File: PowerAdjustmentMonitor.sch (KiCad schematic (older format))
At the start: 11 parts

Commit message: Put the power schematic in the wrong sub-module (PowerAdjustmentMonitor)
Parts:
- removed C? (x2): C, ~, symbol C
- removed F? (x4): FUSE, ~, symbol FUSE
- removed L? (x2): INDUCTOR, ~, symbol INDUCTOR
- removed P?: CONN_12X2, symbol CONN_12X2
- removed R?: R, ~, symbol R
- removed SW?: SWITCH_INV, ~, symbol SWITCH_INV

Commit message: 3.7 Understanding The Power Control, Conditioning And Monitoring Module     Prior to addition of adjustable resistor. Acidently did save-whole-project
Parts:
- added JP? (x3): JUMPER, symbol JUMPER
- added R? (x10): R, symbol R
- added U? (x2): 7805, symbol 7805
- added U? (x2): LM317K, TO-3, symbol LM317K
- added U? (x2): LM324, symbol LM324
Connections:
- net labels added: +12V, +3.3V, +5V, -12V, 3V3_MON, 5V5_MON, AGND, FE_V+, FE_V-, GND, V+_ADJ_MON, V+_CURR_MON, V+_MON, V-_ADJ, V-_ADJ_MON, V-_CURR_MON, V-_MON
- wire segments 0 -> 87

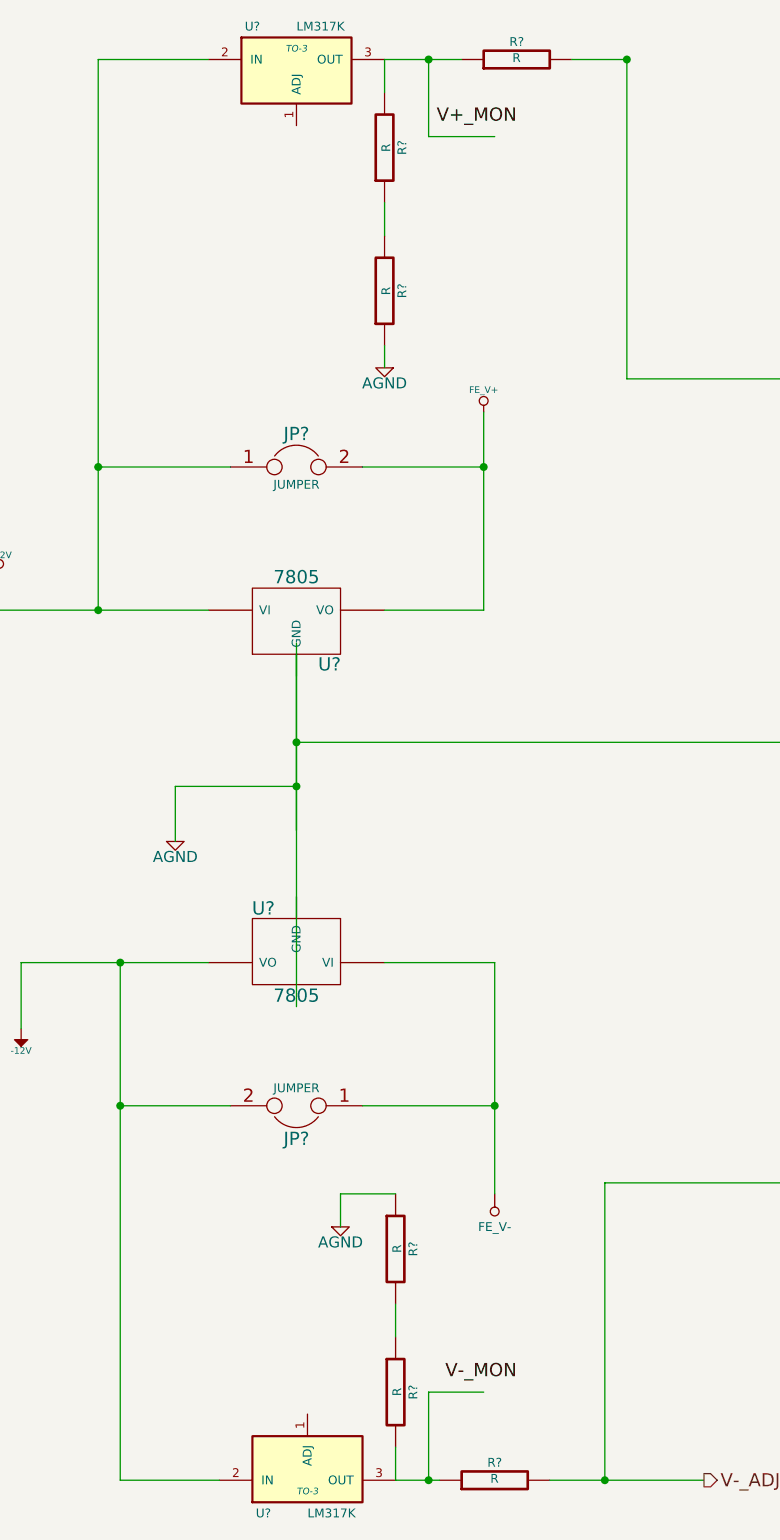
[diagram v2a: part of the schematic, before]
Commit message: Added variable resistor(s) to LM317's output
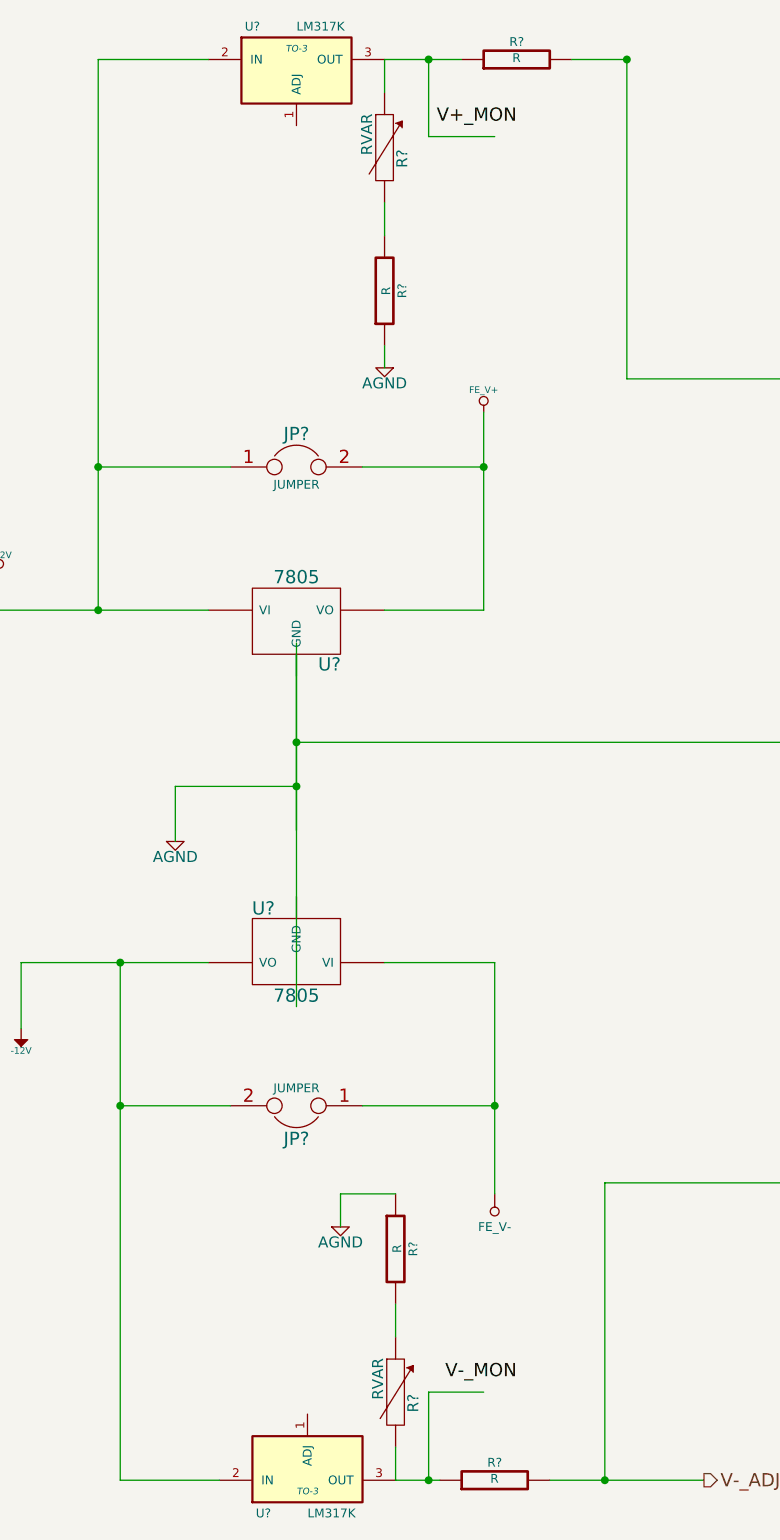
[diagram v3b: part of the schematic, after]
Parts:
- removed R? (x2): R, symbol R
- added R? (x2): RVAR, symbol RVAR
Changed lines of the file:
@@
-$Comp
-L R R?
-U 1 1 52F50F67
-P 4300 6850
-F 0 "R?" V 4380 6850 40  0000 C CNN
-F 1 "R" V 4307 6851 40  0000 C CNN
-F 2 "" V 4230 6850 30  0000 C CNN
-F 3 "" H 4300 6850 30  0000 C CNN
-	1    4300 6850
-	1    0    0    -1
-$EndComp
 $Comp
 L R R?
@@
 $Comp
 L R R?
-U 1 1 52F51722
-P 4250 1200
-F 0 "R?" V 4330 1200 40  0000 C CNN
-F 1 "R" V 4257 1201 40  0000 C CNN
-F 2 "" V 4180 1200 30  0000 C CNN
-F 3 "" H 4250 1200 30  0000 C CNN
-	1    4250 1200
-	1    0    0    1
-$EndComp
-$Comp
-L R R?
 U 1 1 52F51728
 P 4250 1850
@@
 Text Label 8950 6100 2    60   ~ 0
 V-_MON
+$Comp
+L RVAR R?
+U 1 1 52F526E6
+P 4300 6850
+F 0 "R?" V 4380 6800 50  0000 C CNN
+F 1 "RVAR" V 4220 6910 50  0000 C CNN
+F 2 "" H 4300 6850 60  0000 C CNN
+F 3 "" H 4300 6850 60  0000 C CNN
+	1    4300 6850
+	1    0    0    -1
+$EndComp
+$Comp
+L RVAR R?
+U 1 1 52F526F3
+P 4250 1200
+F 0 "R?" V 4330 1150 50  0000 C CNN
+F 1 "RVAR" V 4170 1260 50  0000 C CNN
+F 2 "" H 4250 1200 60  0000 C CNN
+F 3 "" H 4250 1200 60  0000 C CNN
+	1    4250 1200
+	1    0    0    -1
+$EndComp
 $EndSCHEMATC

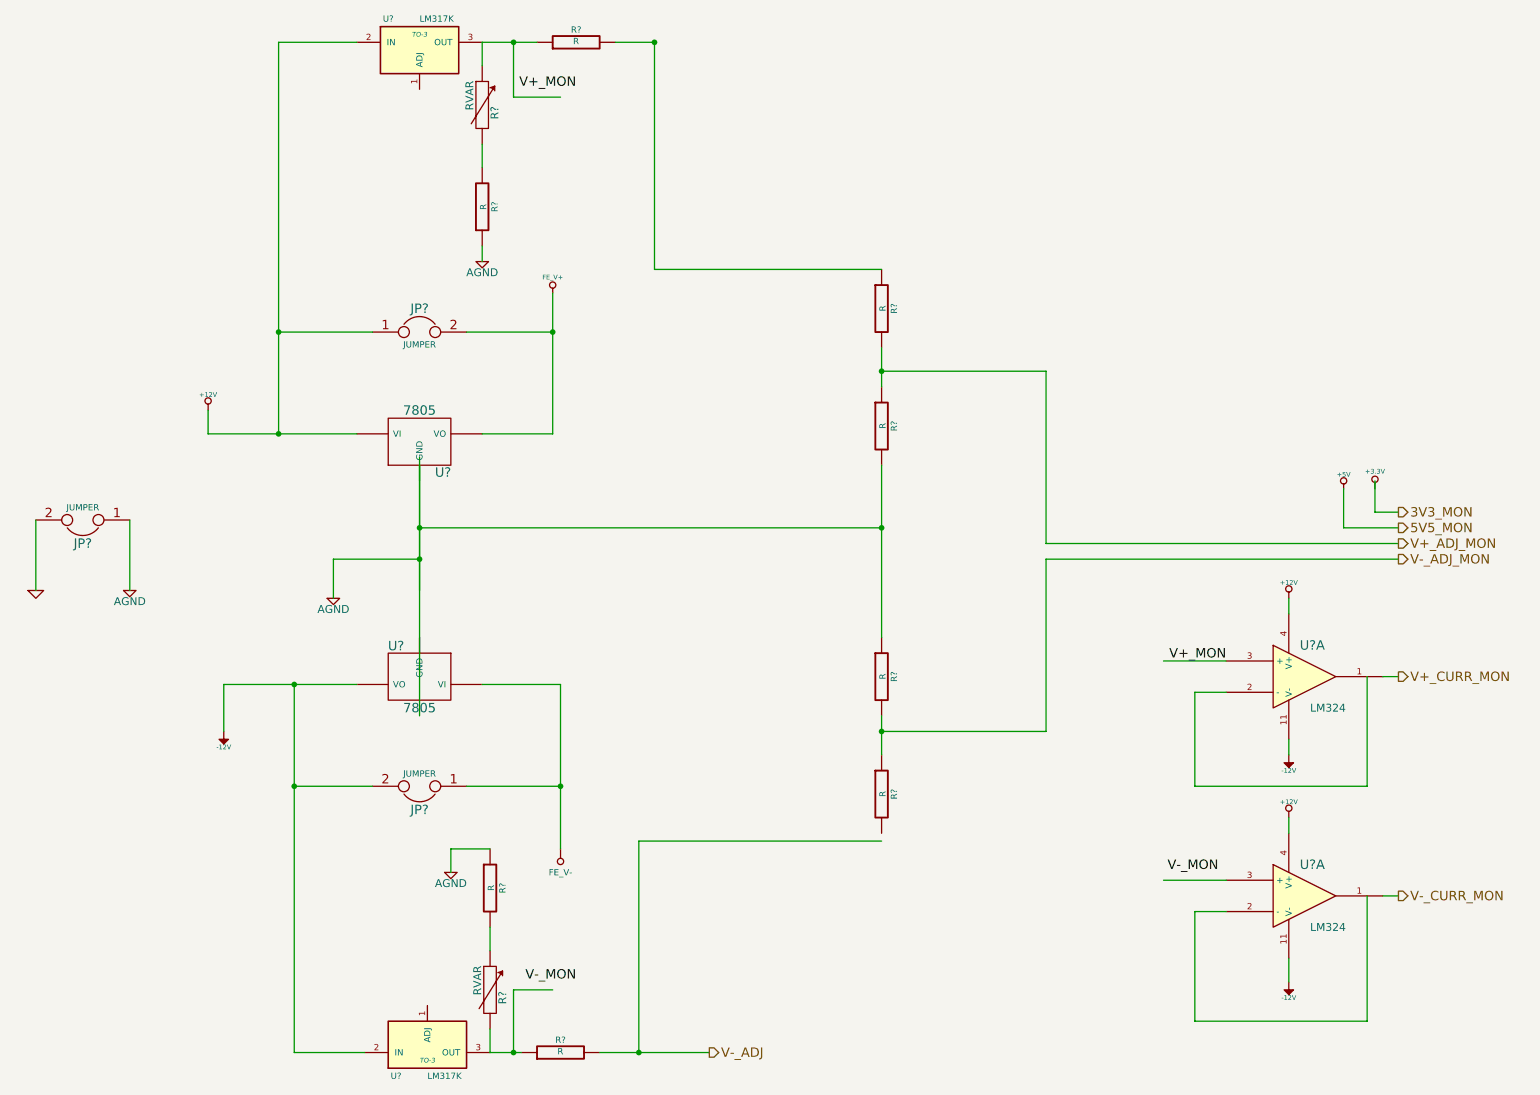
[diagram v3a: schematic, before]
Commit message: Forgot the V+_ADJ pin, fixed
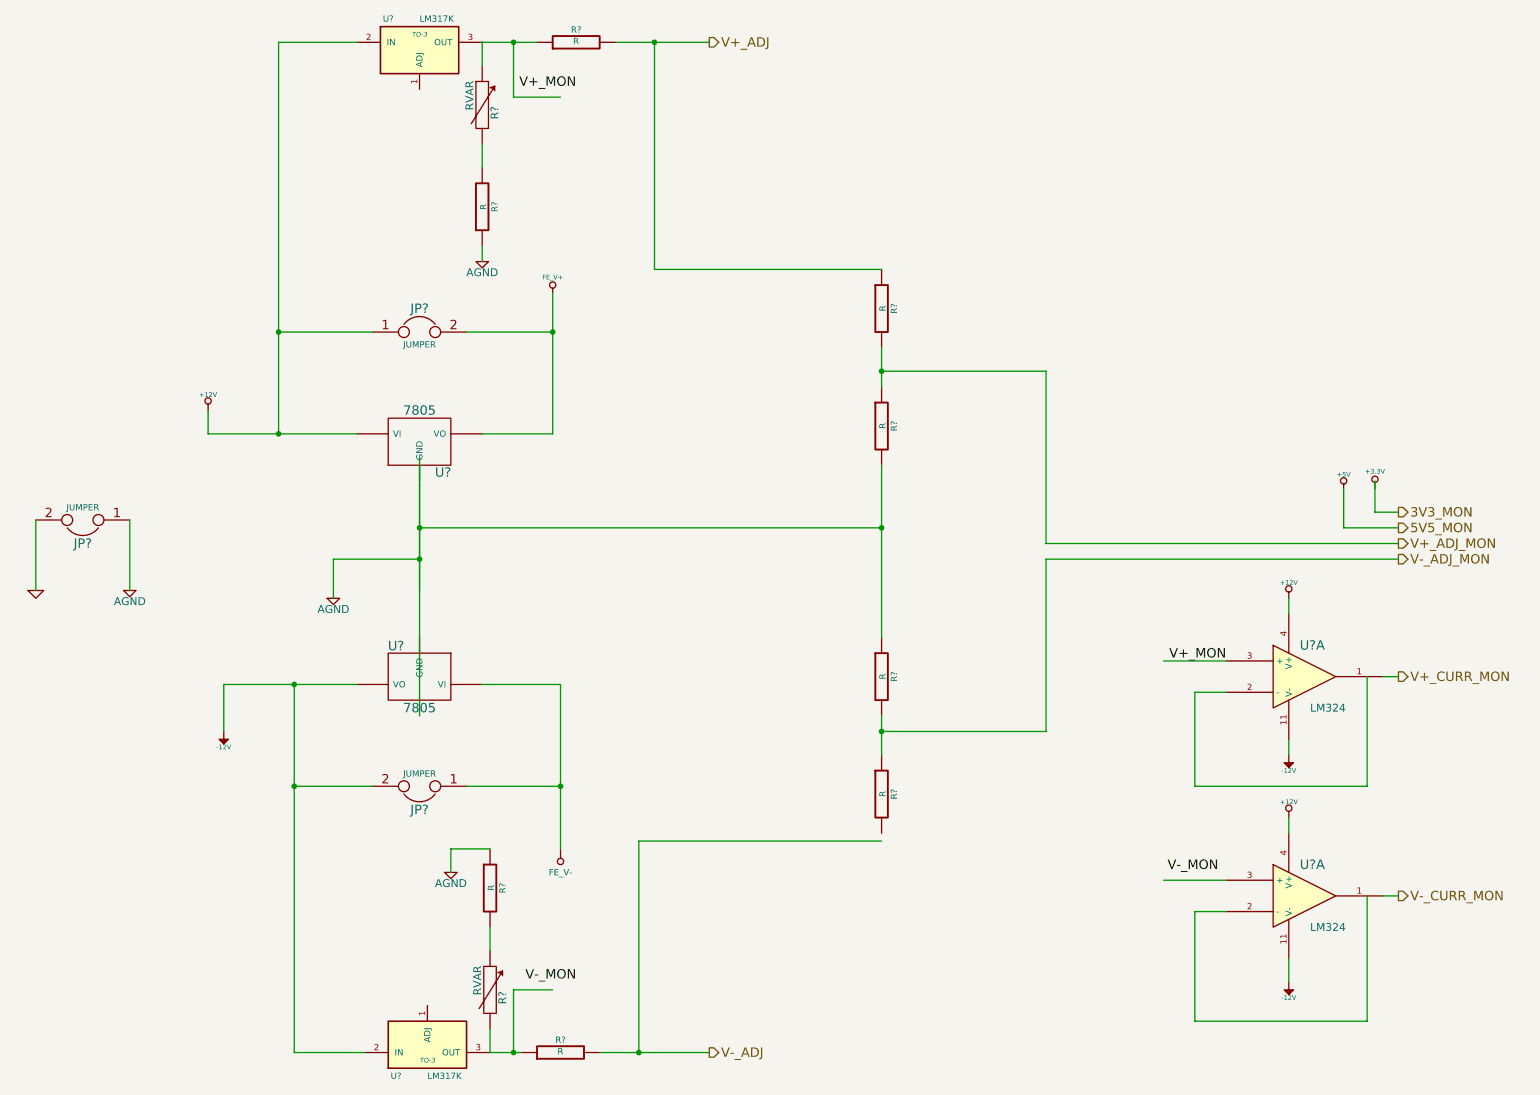
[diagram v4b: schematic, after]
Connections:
- net labels added: V+_ADJ
- wire segments 87 -> 71
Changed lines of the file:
@@
 	3550 2650 2950 2650
 Wire Wire Line
-	2950 800  2950 2650
-Wire Wire Line
-	2950 2650 2950 3300
-Wire Wire Line
-	2500 3300 2950 3300
-Wire Wire Line
-	2950 3300 3450 3300
+	2950 800  2950 3300
+Wire Wire Line
+	2500 3300 3450 3300
 Wire Wire Line
 	4150 2650 4700 2650
 Wire Wire Line
-	4700 2400 4700 2650
-Wire Wire Line
-	4700 2650 4700 3300
+	4700 2400 4700 3300
 Wire Wire Line
 	4700 3300 4250 3300
 Wire Wire Line
-	3850 3450 3850 3900
-Wire Wire Line
-	3850 3900 3850 4100
-Wire Wire Line
-	3850 4100 3850 4300
-Wire Wire Line
-	3850 3500 3850 3900
-Wire Wire Line
-	3850 3900 3850 4100
-Wire Wire Line
-	3850 4100 3850 5100
+	3850 3450 3850 4300
+Wire Wire Line
+	3850 3500 3850 5100
 Wire Wire Line
 	3300 4350 3300 4100
@@
 Connection ~ 3850 4100
 Wire Wire Line
-	2600 4900 3050 4900
-Wire Wire Line
-	3050 4900 3450 4900
-Wire Wire Line
-	3050 4900 3050 5550
-Wire Wire Line
-	3050 5550 3050 7250
+	2600 4900 3450 4900
+Wire Wire Line
+	3050 4900 3050 7250
 Wire Wire Line
 	3050 5550 3550 5550
@@
 	4250 4900 4750 4900
 Wire Wire Line
-	4750 4900 4750 5550
-Wire Wire Line
-	4750 5550 4750 5950
+	4750 4900 4750 5950
 Wire Wire Line
 	4750 5550 4150 5550
@@
 	4050 5950 4050 6100
 Wire Wire Line
-	5000 7250 5250 7250
-Wire Wire Line
-	5250 7250 5700 7250
+	5000 7250 5700 7250
 Wire Wire Line
 	2950 800  3450 800
@@
 Connection ~ 5350 800
 Wire Wire Line
-	6800 3500 6800 3900
-Wire Wire Line
-	6800 3900 6800 4600
+	6800 3500 6800 4600
 Wire Wire Line
 	6800 3900 3850 3900
 Connection ~ 3850 3900
 Wire Wire Line
-	6800 2750 6800 2900
-Wire Wire Line
-	6800 2900 6800 3000
+	6800 2750 6800 3000
 $Comp
 L R R?
@@
 $EndComp
 Wire Wire Line
-	6800 5100 6800 5200
-Wire Wire Line
-	6800 5200 6800 5350
+	6800 5100 6800 5350
 Connection ~ 6800 3900
 Wire Wire Line
@@
 $EndComp
 Wire Wire Line
-	4500 7250 4450 7250
-Wire Wire Line
-	4450 7250 4300 7250
+	4300 7250 4500 7250
 $Comp
 L R R?
@@
 $EndComp
 Wire Wire Line
-	5350 800  5100 800
-Wire Wire Line
-	4600 800  4450 800
-Wire Wire Line
-	4450 800  4250 800
+	5100 800  5700 800
+Wire Wire Line
+	4250 800  4600 800
 Wire Wire Line
 	4450 7250 4450 6850
@@
 	1    0    0    -1
 $EndComp
+Text HLabel 5700 800  2    60   Output ~ 0
+V+_ADJ
 $EndSCHEMATC

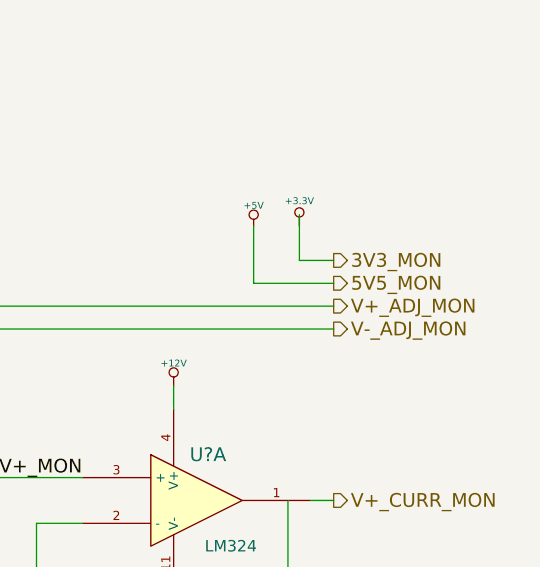
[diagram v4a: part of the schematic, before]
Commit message: fixed pin name typo 5V5_MON => 5V_MON
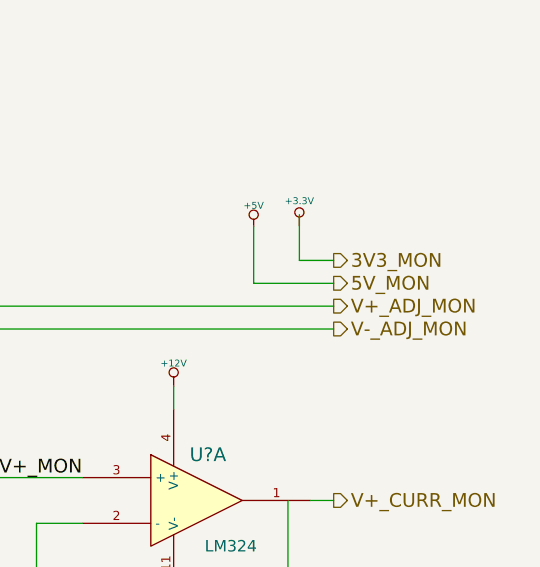
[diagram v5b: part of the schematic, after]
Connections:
- net labels added: 5V_MON
- net labels removed: 5V5_MON
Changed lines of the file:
@@
 3V3_MON
 Text HLabel 10100 3900 2    60   Output ~ 0
-5V5_MON
+5V_MON
 Text HLabel 10100 4000 2    60   Output ~ 0
 V+_ADJ_MON
